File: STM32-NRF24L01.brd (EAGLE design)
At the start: 49.5 x 23 mm, 21 parts, among them IC1 STM32F030K6T6, IC2 MCP73811/2, IC3 SPX3819M5_3_3, J1 61301411121, J2 61301411121, P1 PUSH-SMD

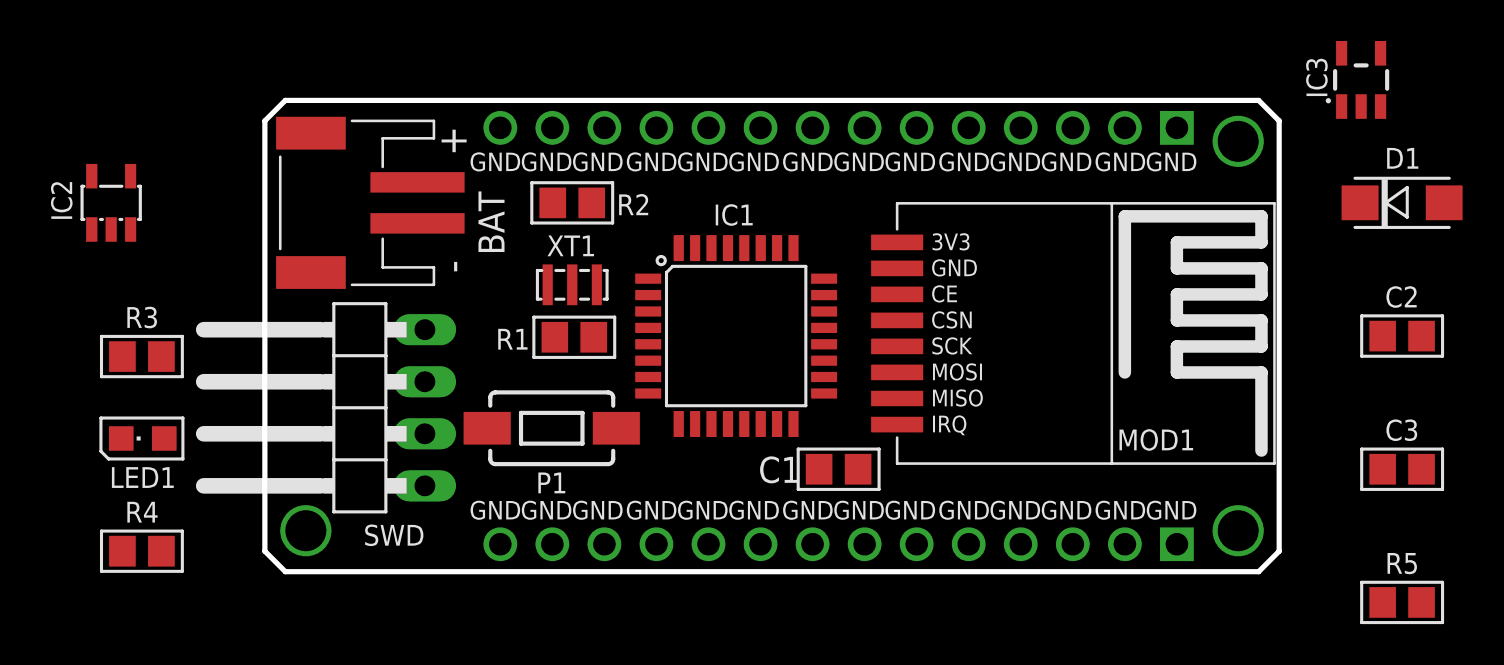
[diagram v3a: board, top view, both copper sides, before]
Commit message: Terminado SCH, Inicio BRD
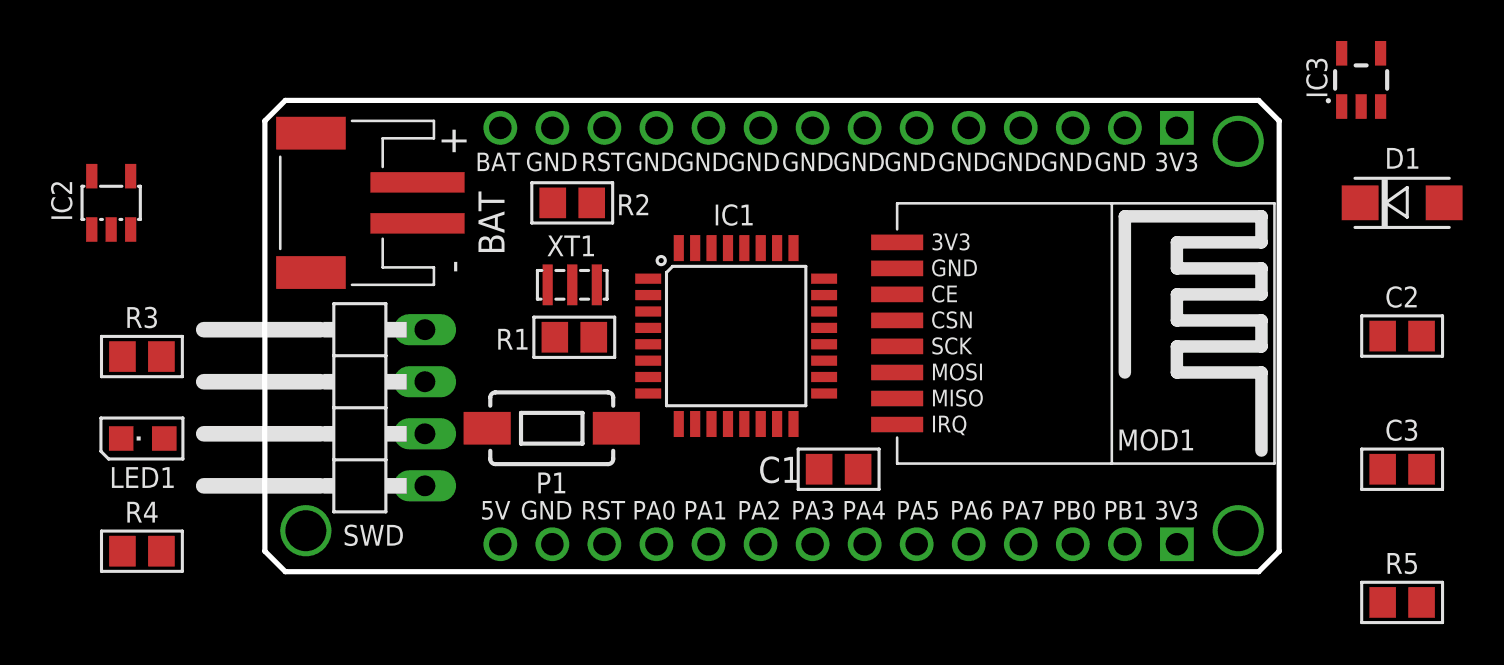
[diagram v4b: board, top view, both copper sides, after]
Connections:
- removed net PB0(AN8): IC1.14
- removed net PB1(AN9): IC1.15
- new net PB0: IC1.14, J1.3
- new net PB1: IC1.15, J1.2
- net +3V3: now also J1.1, J2.1
- net +5V: now also J1.14
- net AN0: now also J1.11
- net AN1: now also J1.10
- net AN2: now also J1.9
- net AN3: now also J1.8
- net AN4: now also J1.7
- net AN5: now also J1.6
- net AN6: now also J1.5
- net AN7: now also J1.4
- net GND: now also J1.13, J2.13; no longer J1.14, J2.14
- net MISO: now also J2.8
- net MOSI: now also J2.9
- net PA11: now also J2.5
- net PA12: now also J2.6
- net PA8: now also J2.2
- net RST: now also J1.12, J2.12
- net RX: now also J2.4
- net SCK: now also J2.7
- net SCL: now also J2.10
- net SDA: now also J2.11
- net TX: now also J2.3
- net V+: now also J2.14
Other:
- board text added: "3V3"
- board text added: "5V"
- board text added: "BAT"
- board text added: "PA0"
- board text added: "PA1"
- board text added: "PA2"
- board text added: "PA3"
- board text added: "PA4"
- board text added: "PA5"
- board text added: "PA6"
- board text added: "PA7"
- board text added: "PB0"
- board text added: "PB1"
- board text added: "RST"

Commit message: Posicionado componentes, inicio ruteo
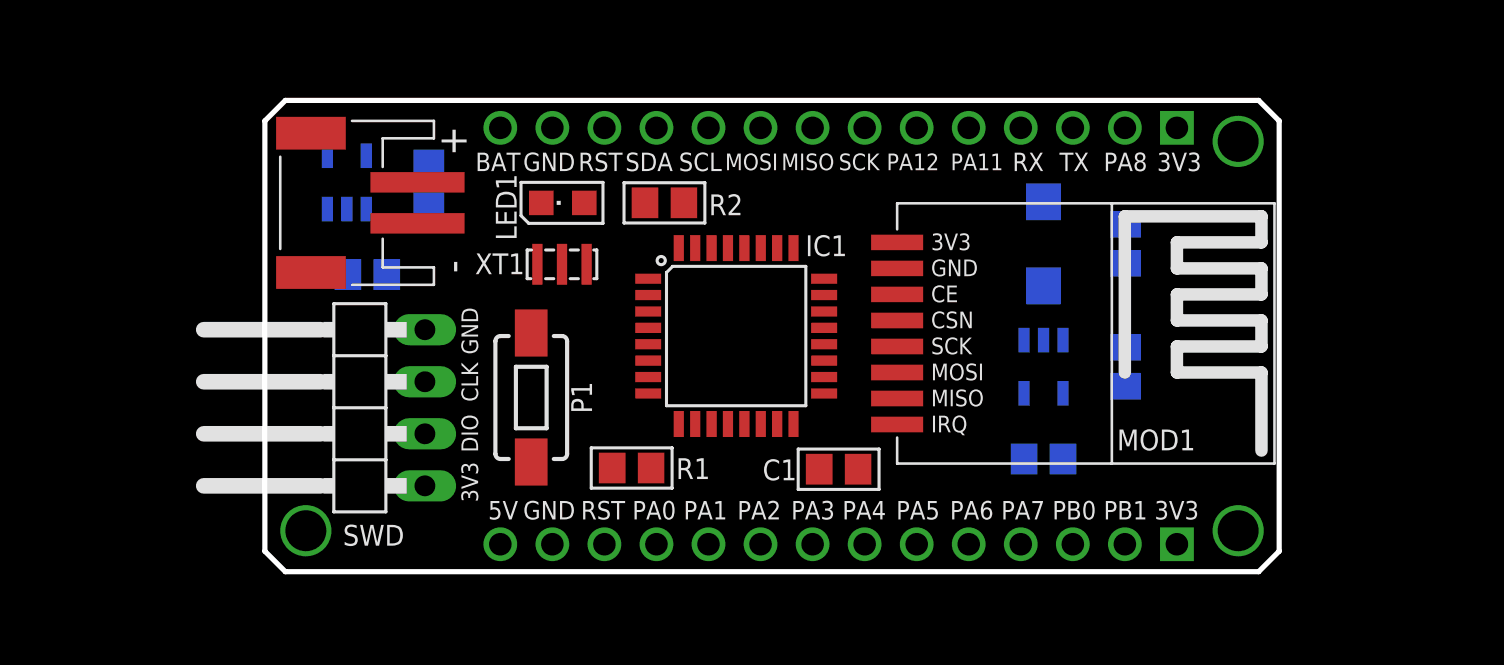
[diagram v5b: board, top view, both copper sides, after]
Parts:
- moved LED1 23.5 mm to (14.5, 18.0)
- moved R4 22.8 mm to (8.00, 19.0), flipped to the bottom, turned to 270 degrees
- moved IC3 20.9 mm to (38.0, 10.0), flipped to the bottom, turned to 180 degrees
- moved R5 17.7 mm to (42.0, 10.0), flipped to the bottom, turned to 90 degrees
- moved D1 17.6 mm to (38.0, 16.0), flipped to the bottom, turned to 90 degrees
- moved C3 17.5 mm to (38.0, 5.50), flipped to the bottom, turned to 180 degrees
- moved C2 14.2 mm to (42.0, 16.0), flipped to the bottom, turned to 270 degrees
- moved R3 11.7 mm to (5.00, 14.5), flipped to the bottom
- moved IC2 11.5 mm to (4.00, 19.0), flipped to the bottom
- moved R1 6.97 mm to (17.9, 5.06), turned to 180 degrees
- moved R2 4.50 mm to (19.5, 18.0)
- moved P1 1.80 mm to (13.0, 8.50), turned to 90 degrees
- moved XT1 1.12 mm to (14.5, 15.0)
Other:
- board text added: "CLK"
- board text added: "DIO"
- board text added: "MISO"
- board text added: "MOSI"
- board text added: "PA11"
- board text added: "PA12"
- board text added: "PA8"
- board text added: "RX"
- board text added: "SCK"
- board text added: "SCL"
- board text added: "SDA"
- board text added: "TX"

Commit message: Ruteo al 50%
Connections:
- removed net PA11: IC1.21, J2.5
- removed net PA12: IC1.22, J2.6
- removed net PA8: IC1.18, J2.2
- net CE: now also IC1.22, J2.6
- net CSN: now also IC1.21, J2.5; no longer MOD1.5
- net IRQ: now also IC1.18, J2.2
- net NSS: now also MOD1.5
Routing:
- net +3V3: track 0.00 -> 52.4 mm
- net SCK: track 0.00 -> 29.4 mm, vias 0 -> 1
- net MISO: track 0.00 -> 23.6 mm, vias 0 -> 1
- net SWDIO: track 0.00 -> 22.3 mm, vias 0 -> 1
- net SWCLK: track 0.00 -> 21.6 mm, vias 0 -> 1
- net PB1: track 0.00 -> 21.3 mm
- net PB0: track 0.00 -> 19.4 mm
- net NSS: track 0.00 -> 18.9 mm, vias 0 -> 2
- net RST: track 0.00 -> 17.5 mm
- net AN7: track 0.00 -> 17.5 mm
- net CSN: track 0.00 -> 16.7 mm, vias 0 -> 2
- net AN6: track 0.00 -> 16.5 mm, vias 0 -> 1
- net CE: track 0.00 -> 14.4 mm
- net AN5: track 0.00 -> 14.3 mm, vias 0 -> 1
- net AN4: track 0.00 -> 12.5 mm, vias 0 -> 1
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
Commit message: Terminado Ruteo
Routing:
- net GND: track 9.24 -> 131.9 mm, vias 0 -> 8
- net +5V: track 9.94 -> 95.9 mm, vias 0 -> 2
- net +3V3: track 52.4 -> 131.4 mm, vias 0 -> 5
- net V+: track 5.99 -> 42.2 mm, vias 0 -> 1
- net IRQ: track 0.00 -> 27.1 mm
- net MOSI: track 6.19 -> 29.8 mm, vias 0 -> 2
- net TX: track 0.00 -> 22.3 mm, vias 0 -> 2
- net RX: track 0.00 -> 19.3 mm, vias 0 -> 2
- net RST: track 17.5 -> 36.1 mm, vias 0 -> 1
- net N$7: track 0.00 -> 8.99 mm, vias 0 -> 1
- net SCK: track 29.4 -> 27.1 mm, vias 1 -> 2
- net MISO: track 23.6 -> 24.7 mm, vias 1 -> 2
- net NSS: track 18.9 -> 19.9 mm
- added copper zone on layer 1, net GND
- added copper zone on layer 16, net GND
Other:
- board text added: "CaliBeta STM32 RF Module"
